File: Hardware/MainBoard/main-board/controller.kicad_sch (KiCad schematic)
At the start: 42 parts, among them J11 Conn_01x04, J12 Conn_01x05, J13 Conn_01x04, J14 Conn_01x06, J15 Conn_01x08, J6 Conn_01x07, J7 Conn_01x04, J8 Conn_01x02, J9 Conn_01x02, Q1 IRLML6244TRPBF, Q2 IRLML6244TRPBF, Q3 IRLML6244TRPBF, Q4 IRLML6244TRPBF, SW2 SW_SPDT, U4 STM32F401RETx, Y2 ATS08A-E

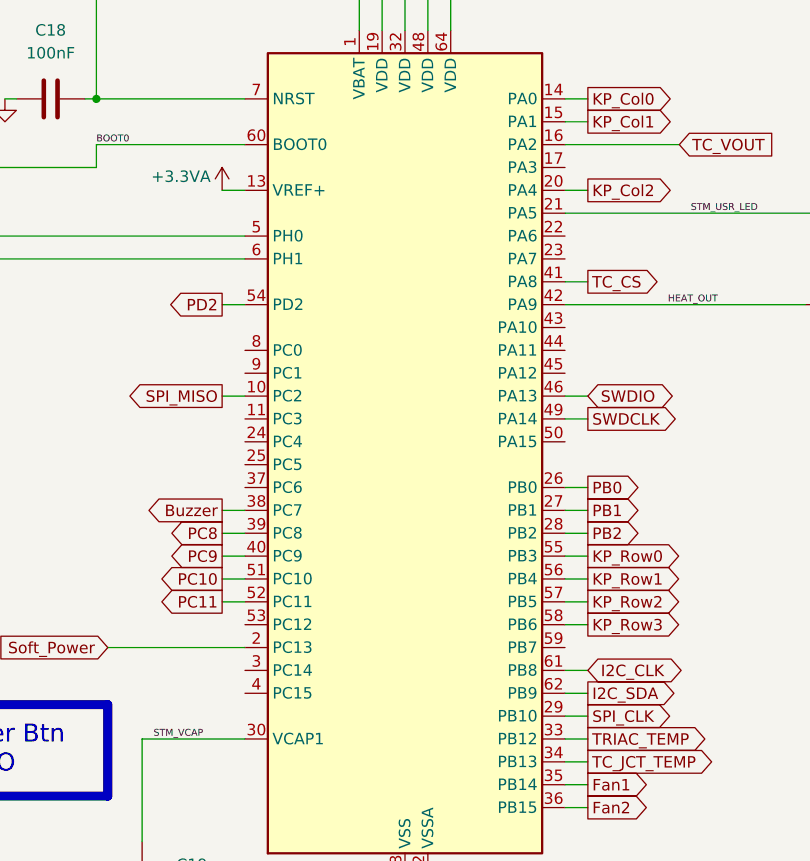
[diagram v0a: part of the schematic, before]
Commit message: edit schematic to pass schematic DRC
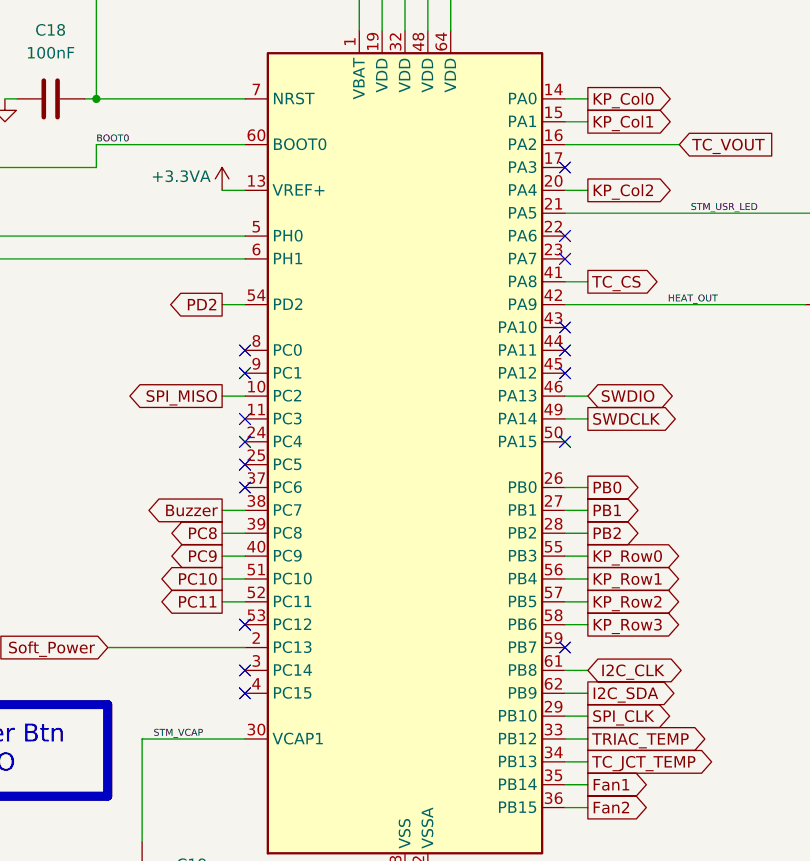
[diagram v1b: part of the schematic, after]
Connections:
- no-connect marks 0 -> 17
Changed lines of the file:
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@@
 		(color 0 0 0 0)
+	)
+	(no_connect
+		(at 195.58 194.31)
+	)
+	(no_connect
+		(at 195.58 171.45)
+	)
+	(no_connect
+		(at 160.02 196.85)
+	)
+	(no_connect
+		(at 195.58 181.61)
+	)
+	(no_connect
+		(at 160.02 186.69)
+	)
+	(no_connect
+		(at 195.58 173.99)
+	)
+	(no_connect
+		(at 160.02 214.63)
+	)
+	(no_connect
+		(at 160.02 191.77)
+	)
+	(no_connect
+		(at 160.02 222.25)
+	)
+	(no_connect
+		(at 195.58 217.17)
+	)
+	(no_connect
+		(at 160.02 199.39)
+	)
+	(no_connect
+		(at 160.02 194.31)
+	)
+	(no_connect
+		(at 195.58 184.15)
+	)
+	(no_connect
+		(at 160.02 219.71)
+	)
+	(no_connect
+		(at 195.58 163.83)
+	)
+	(no_connect
+		(at 195.58 186.69)
+	)
+	(no_connect
+		(at 160.02 184.15)
 	)
 	(wire

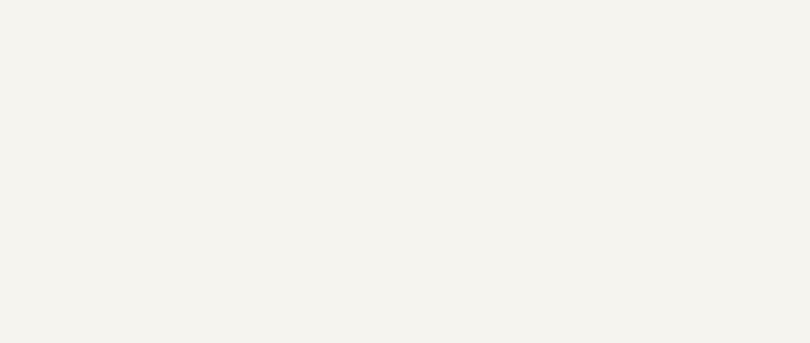
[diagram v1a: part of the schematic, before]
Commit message: add details, need to change TC amp gain for different voltage and temperature
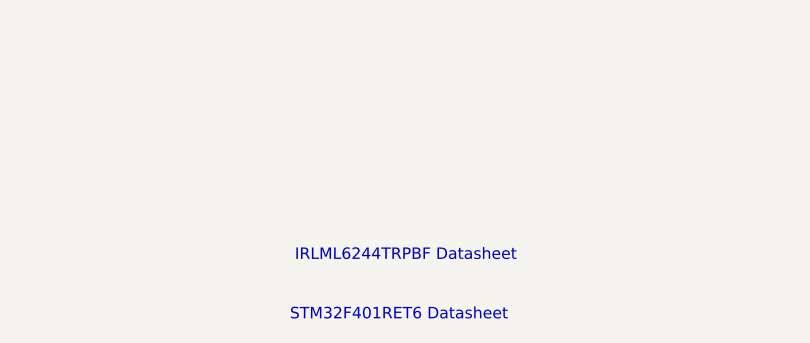
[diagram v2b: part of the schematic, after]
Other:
- note added: "IRLML6244TRPBF Datasheet"
- note added: "STM32F401RET6 Datasheet"
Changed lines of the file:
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@@
+		)
+	)
+	(text "STM32F401RET6 Datasheet"
+		(exclude_from_sim no)
+		(at 277.368 256.794 0)
+		(effects
+			(font
+				(size 1.27 1.27)
+			)
+			(href "https://www.st.com/content/ccc/resource/technical/document/datasheet/30/91/86/2d/db/94/4a/d6/DM00102166.pdf/files/DM00102166.pdf/jcr:content/translations/en.DM00102166.pdf")
 		)
 	)
@@
 		)
 	)
+	(text "IRLML6244TRPBF Datasheet"
+		(exclude_from_sim no)
+		(at 278.13 250.19 0)
+		(effects
+			(font
+				(size 1.27 1.27)
+			)
+			(href "https://www.infineon.com/dgdl/irlml6244pbf.pdf?fileId=5546d462533600a4015356686fed261f")
+		)
+	)

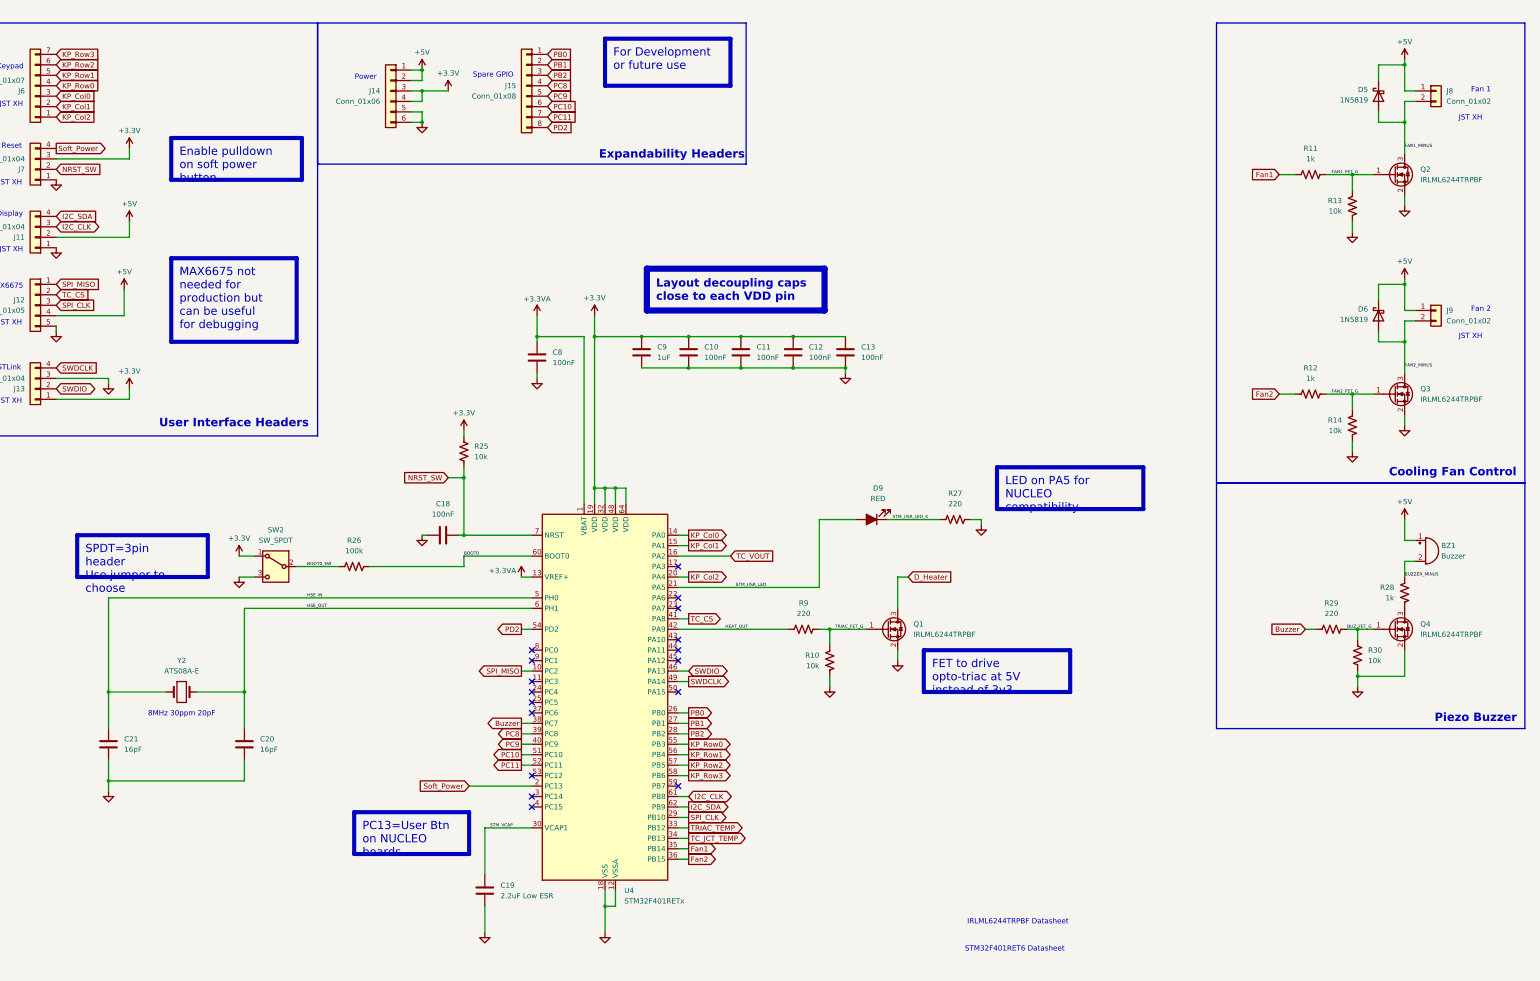
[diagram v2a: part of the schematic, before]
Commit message: add heatsink mounting holes, change a few footprints, clean up schematic
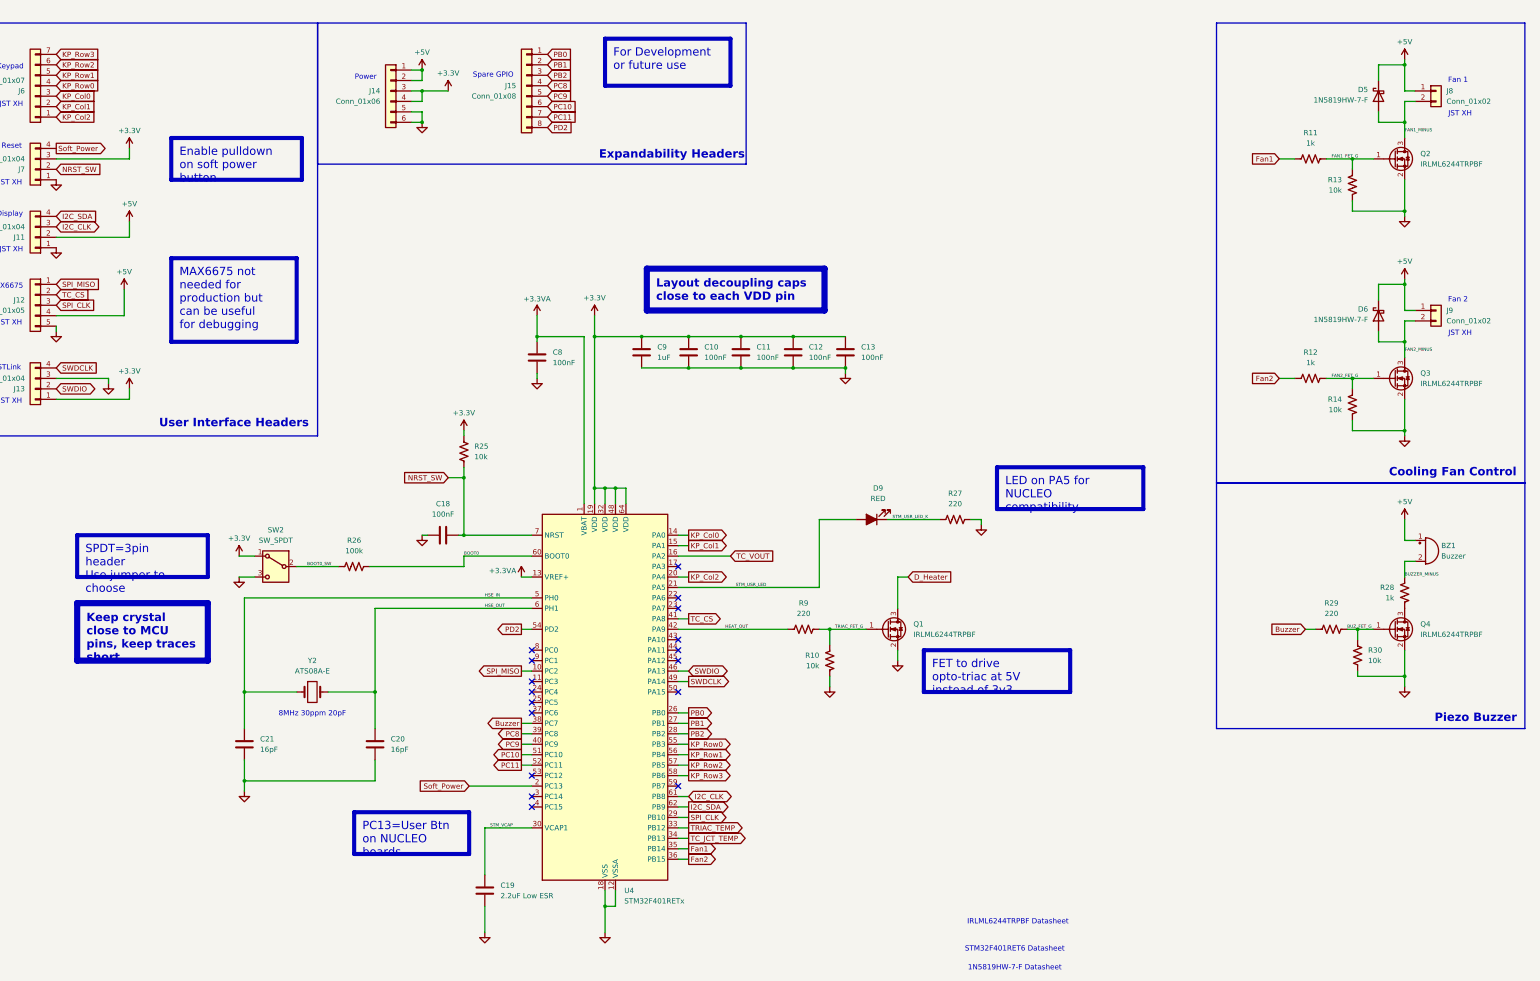
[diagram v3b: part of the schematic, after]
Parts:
- D5, D6: value 1N5819 -> 1N5819HW-7-F; footprint Diode_THT:D_DO-41_SOD81_P10.16mm_Horizontal -> Diode_SMD:D_SOD-123
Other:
- note added: "1N5819HW-7-F Datasheet"
- moved on the sheet: C20, C21, Q2, Q3, R11, R12, R13, R14, Y2

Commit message: working on PCB layout
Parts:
- added D10: 1N5819HW-7-F, Diode_SMD:D_SOD-123, symbol Diode:1N5819
- added J16: Conn_01x03, Connector_JST:JST_XH_B3B-XH-A_1x03_P2.50mm_Vertical, symbol Connector_Generic:Conn_01x03
- added Q5: IRLML6244TRPBF, Package_TO_SOT_SMD:SOT-23, symbol Transistor_FET:IRLML6244
- added R31: 1k, Resistor_SMD:R_0603_1608Metric_Pad0.98x0.95mm_HandSolder, symbol Device:R_US
- added R32: 10k, Resistor_SMD:R_0603_1608Metric_Pad0.98x0.95mm_HandSolder, symbol Device:R_US
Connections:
- net +5V: now also D10.1 (K), J16.3 (Pin_3)
- net FAN2_FET_G: now also Q5.1 (G), R31.2, R32.1
- net FAN2_MINUS: now also D10.2 (A), J16.2 (Pin_2), Q5.3 (D)
- net GND: now also Q5.2 (S), R32.2
- net Fan3: now reaches U4.59 (PB7)
- net Fan3: now also R31.1
- new net Fan3_Sense: J16.1 (Pin_1)
- no-connect marks 17 -> 16
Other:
- note added: "Enclosure Fans"
- note added: "TRIAC Fan"
- note removed: "Cooling Fan Control"
- moved on the sheet: BZ1, D5, D6, J8, J9, Q2, Q3, Q4, R11, R12, R13, R14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

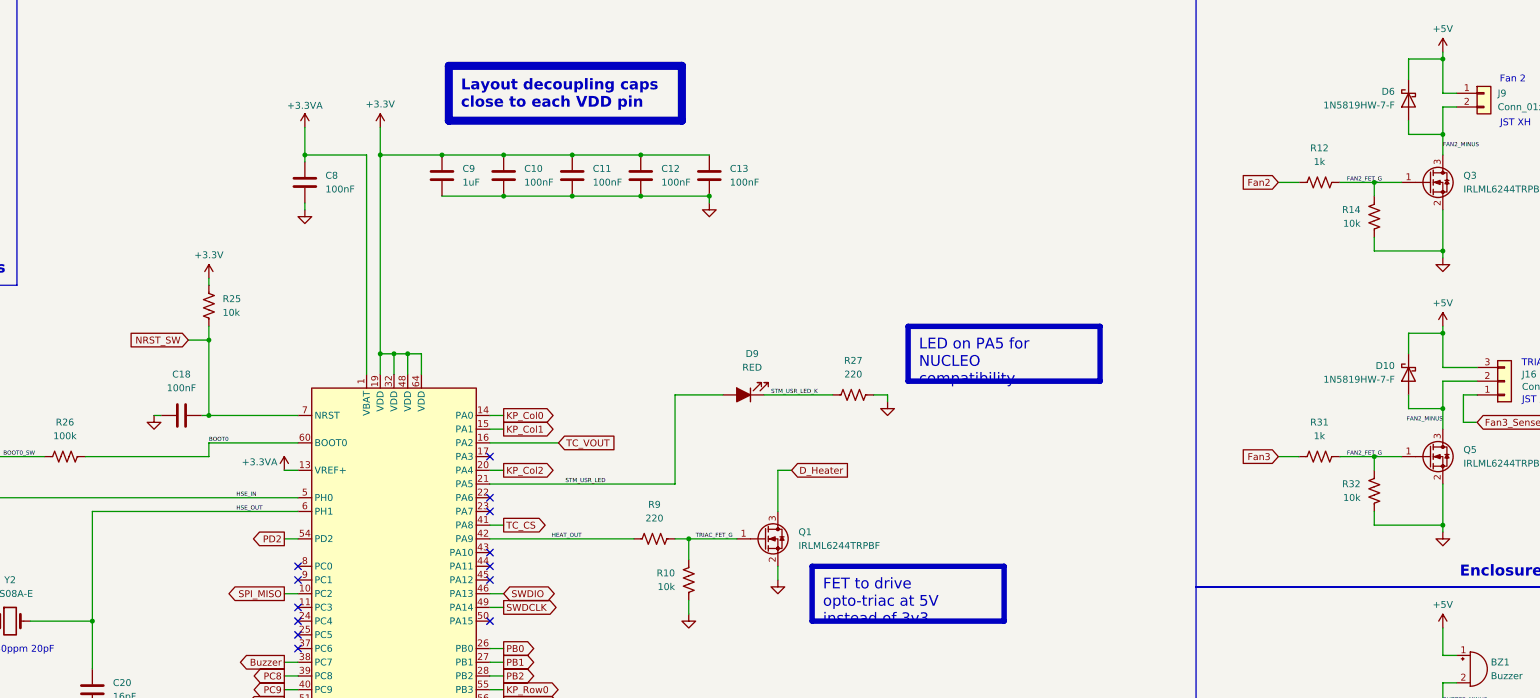
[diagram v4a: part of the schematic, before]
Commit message: routing halfway done, trying autorouter to finish low voltage signals
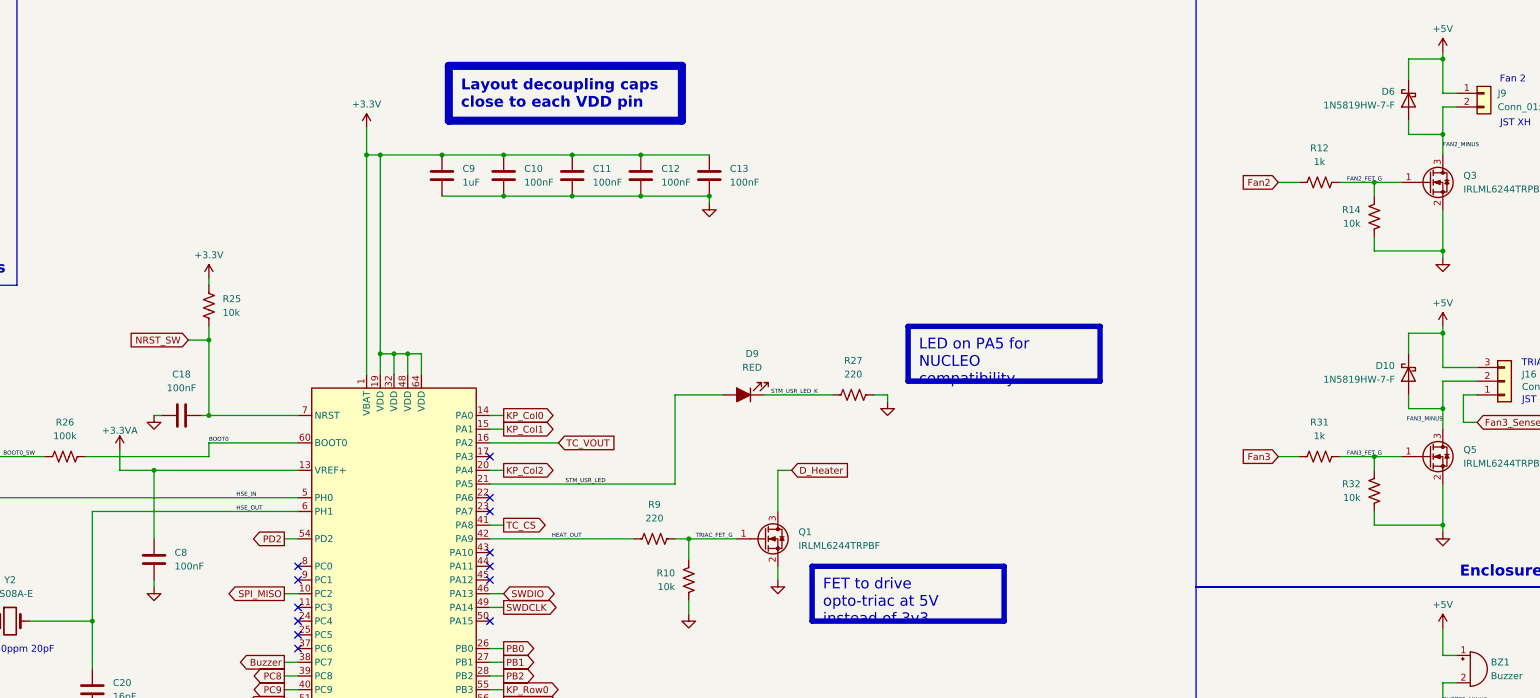
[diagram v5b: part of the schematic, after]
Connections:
- net +3.3V: now also U4.1 (VBAT)
- net +3.3VA: no longer U4.1 (VBAT)
- net FAN2_FET_G: no longer Q5.1 (G), R31.2, R32.1
- net FAN2_MINUS: no longer D10.2 (A), J16.2 (Pin_2), Q5.3 (D)
- new net FAN3_FET_G: Q5.1 (G), R31.2, R32.1
- new net FAN3_MINUS: D10.2 (A), J16.2 (Pin_2), Q5.3 (D)

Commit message: Finish board layout
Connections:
- net KP_Col0: now also J6.1 (Pin_1); no longer J6.3 (Pin_3)
- net KP_Col2: now also J6.3 (Pin_3); no longer J6.1 (Pin_1)
- net PB0: now also J15.3 (Pin_3); no longer J15.1 (Pin_1)
- net PB1: now also J15.4 (Pin_4); no longer J15.2 (Pin_2)
- net PB2: now also J15.5 (Pin_5); no longer J15.3 (Pin_3)
- net PC8: now also J15.2 (Pin_2); no longer J15.4 (Pin_4)
- net PC9: now also J15.1 (Pin_1); no longer J15.5 (Pin_5)
